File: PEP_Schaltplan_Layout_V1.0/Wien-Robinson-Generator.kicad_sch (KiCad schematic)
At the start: 14 parts, among them Q5 BF256, U13 LT1819

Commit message: Bauoptionen1
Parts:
- removed C24: 100µ, Capacitor_THT:CP_Radial_D13.0mm_P5.00mm, symbol ltspice:cap
- removed Q5: BF256, Package_TO_SOT_THT:TO-92L_Inline, symbol BF256:BF256
- removed R29: 13.75k, Resistor_SMD:R_1206_3216Metric, symbol ltspice:res
- removed R30: 20k, Resistor_SMD:R_1206_3216Metric, symbol ltspice:res
- added C29, C30, C31, C32, C33, C34, C35, C36, C37, C38, C39, C40, C41, C42: 6.8n, Capacitor_SMD:C_1206_3216Metric, symbol ltspice:cap
- added D17: 1N4148, Diode_THT:D_DO-41_SOD81_P10.16mm_Horizontal, symbol ltspice:diode
- added R44: 10k, Resistor_SMD:R_1206_3216Metric, symbol ltspice:res
- added R50, R51, R52, R53, R54: 0, Resistor_SMD:R_1206_3216Metric, symbol ltspice:res
- added RV3: R_Potentiometer_Dual_Separate, Potentiometer_THT:Potentiometer_Piher_T-16H_Double_Horizontal, symbol Device:R_Potentiometer_Dual_Separate
- added SW1, SW2, SW3, SW4, SW5, SW6: SW_DIP_x04, Button_Switch_THT:SW_DIP_SPSTx04_Slide_6.7x11.72mm_W7.62mm_P2.54mm_LowProfile, symbol Switch:SW_DIP_x04
- R27, R31: value 2k2 -> 500
- R28: value 2k -> 10k
- R32: value 20k -> 0
- R33: value 22k -> 24K
- R34: value 16k -> 12k
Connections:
- net 0: now also C29.2, C30.2, C31.2, C32.2, C33.2, C34.2, C35.2, R52.2
- net Sinus: now also D11.2 (-), D17.1 (+), R54.1, SW3.5, SW3.6, SW3.7, SW3.8, SW4.5, SW4.6, SW4.7, SW4.8
- net at R31.2, U13.3 (+): now also RV3.2, SW1.5, SW1.6, SW1.7, SW1.8, SW2.5, SW2.6, SW2.7, SW2.8; no longer C23.1
- net at R34.2: now also R33.2, R44.1
- net at R27.1: now also R50.2
- net at R28.1, U13.2 (-): now also R51.2; no longer R33.2
- net at R28.2: now also R52.1
- net at C25.2: now also SW5.8; no longer R32.1
- net at D11.1 (+): now also D17.2 (-), R53.1; no longer R34.1
- new net: C39.1, SW4.1
- new net: C40.1, SW4.2
- new net: C41.1, SW4.3
- new net: C42.1, SW4.4
- new net: C23.1, SW1.1
- new net: C30.1, SW1.3
- new net: R33.1, R53.2
- new net: C32.1, SW2.1
- new net: C35.1, SW2.4
- new net: C36.1, SW3.2
- new net: C36.2, SW5.7
- new net: C25.1, SW3.1
- new net: R32.1, RV3.4
- new net: RV3.5, SW5.1, SW5.2, SW5.3, SW5.4, SW6.1, SW6.2, SW6.3, SW6.4
- new net: R50.1, RV3.1
- new net: R44.2, R51.1
- new net: C31.1, SW1.4
- new net: C38.2, SW5.5
- new net: C37.2, SW5.6
- new net: C39.2, SW6.8
- new net: C42.2, SW6.5
- new net: C33.1, SW2.2
- new net: C40.2, SW6.7
- new net: C37.1, SW3.3
- new net: C29.1, SW1.2
- new net: R34.1, R54.2
- new net: C38.1, SW3.4
- new net: C34.1, SW2.3
- new net: C41.2, SW6.6
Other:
- moved on the sheet: C23, D11, R27, R28, R31, R33, R34, U13A, U13C

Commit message: Überarbeitung und Bereinigung
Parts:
- renumbered C29 to C10, C30 to C11, C31 to C12, C32 to C13, C33 to C14, C34 to C15, C35 to C16, C25 to C17, C36 to C18, C37 to C19, C38 to C20, C39 to C21, C40 to C22, C41 to C23, C42 to C24, C23 to C9, D11 to D8, D17 to D9, R52 to R10, R28 to R11, R51 to R12, R44 to R13, R31 to R14, R32 to R15, R33 to R16, R34 to R17, R53 to R18, R54 to R19, R27 to R8, R50 to R9, RV3 to RV1, SW5 to SW3, SW6 to SW4, SW3 to SW5, SW4 to SW6, U13 to U4
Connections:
- net Sinus renamed Sinus_Wien
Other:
- note removed: "R2 und R3 sollen als Doppel potenziometer eingestellt werden jedoch noch mit einem festwider stand von 2k2 damit keine 0 Ohm anliegen können"
- moved on the sheet: C10, C11, C12, C13, C14, C15, C16, C17, C18, C19, C20, C21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

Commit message: Pinheads eingefügt, GND überall (hoffentlich angebunden)
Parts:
- added C10, C9: 100n, Capacitor_SMD:C_1206_3216Metric, symbol ltspice:cap
- added J4: Conn_01x01_Pin, Connector_PinSocket_2.54mm:PinSocket_1x01_P2.54mm_Vertical, symbol Connector:Conn_01x01_Pin
- renumbered C9 to C11, C10 to C12, C11 to C13, C12 to C14, C13 to C15, C14 to C16, C15 to C17, C16 to C18, C17 to C19, C18 to C20, C19 to C21, C20 to C22, C21 to C23, C22 to C24, C23 to C25, C24 to C26, D8 to D10, D9 to D11, R9 to R10, R10 to R11, R11 to R12, R12 to R13, R13 to R14, R14 to R15, R15 to R16, R16 to R17, R17 to R18, R18 to R19, R19 to R20, R8 to R9
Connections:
- net +5V: now also C9.1
- net -5V: now also C10.1
- net 0: now also C10.2, C9.2
- net Sinus_Wien: now also J4.1 (Pin_1)

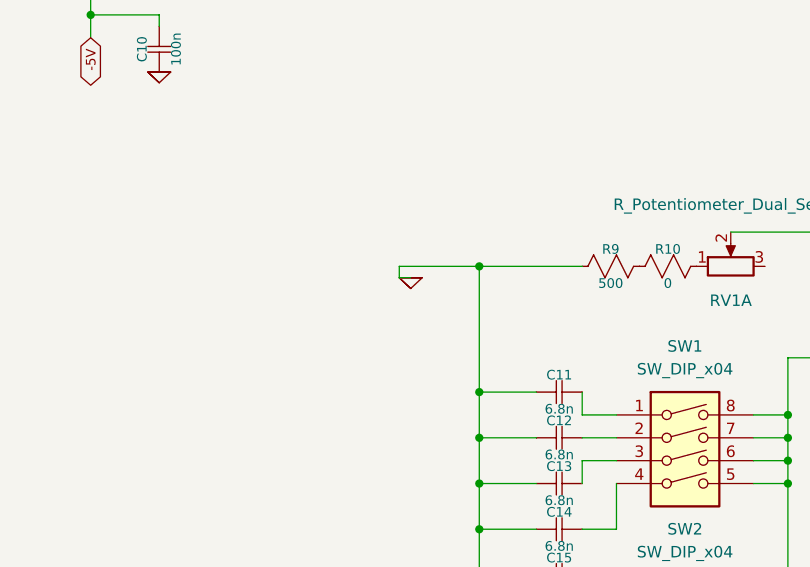
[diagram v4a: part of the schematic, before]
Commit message: Leiterplatten größe definiert und erstes Auto Routing
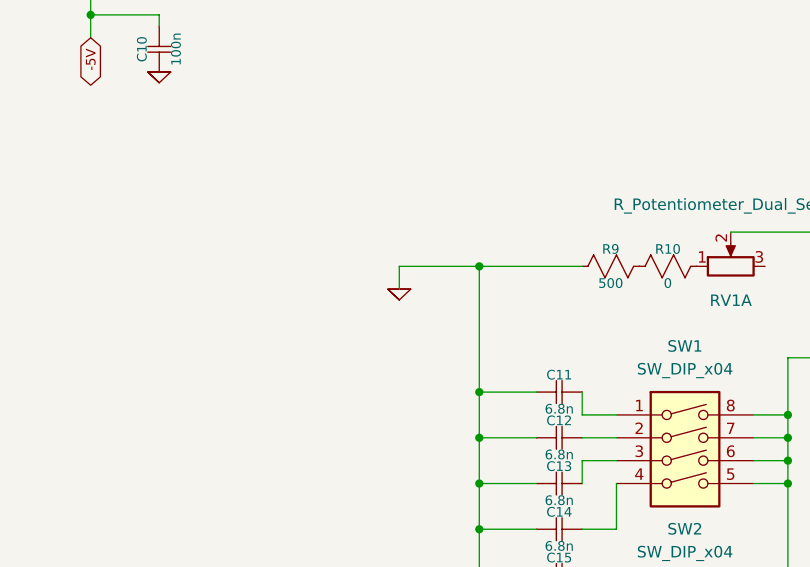
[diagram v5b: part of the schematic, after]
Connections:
- net 0 renamed GND
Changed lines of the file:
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@@
 	(wire
 		(pts
-			(xy 69.85 77.47) (xy 71.12 77.47)
-		)
-		(stroke
-			(width 0.1524)
-			(type solid)
-		)
-	)
-	(wire
-		(pts
 			(xy 229.87 67.31) (xy 229.87 69.85)
 		)
@@
 	(wire
 		(pts
-			(xy 69.85 77.47) (xy 69.85 76.2)
+			(xy 69.85 78.74) (xy 69.85 76.2)
 		)
 		(stroke
@@
 		(at 92.71 135.89 0)
 		(unit 1)
-		(body_style 0)
+		(body_style 1)
 		(exclude_from_sim no)
 		(in_bom yes)
@@
 			)
 		)
-		(property "Value" "0"
+		(property "Value" "GND"
 			(at 92.71 135.89 0)
 			(hide yes)
@@
 	(symbol
 		(lib_id "ltspice:GND")
-		(at 71.12 77.47 0)
+		(at 69.85 78.74 0)
 		(unit 1)
-		(body_style 0)
+		(body_style 1)
 		(exclude_from_sim no)
 		(in_bom yes)
@@
 		(dnp no)
 		(property "Reference" "#GND03"
-			(at 71.12 77.47 0)
+			(at 69.85 78.74 0)
 			(hide yes)
 			(show_name no)
@@
 			)
 		)
-		(property "Value" "0"
-			(at 71.12 77.47 0)
+		(property "Value" "GND"
+			(at 69.85 78.74 0)
 			(hide yes)
 			(show_name no)
@@
 		)
 		(property "Footprint" ""
-			(at 71.12 77.47 0)
+			(at 69.85 78.74 0)
 			(hide yes)
 			(show_name no)
@@
 		)
 		(property "Datasheet" ""
-			(at 71.12 77.47 0)
+			(at 69.85 78.74 0)
 			(hide yes)
 			(show_name no)
@@
 		)
 		(property "Description" ""
-			(at 71.12 77.47 0)
+			(at 69.85 78.74 0)
 			(hide yes)
 			(show_name no)
@@
 		(at 43.18 54.61 0)
 		(unit 1)
-		(body_style 0)
+		(body_style 1)
 		(exclude_from_sim no)
 		(in_bom yes)
@@
 			)
 		)
-		(property "Value" "0"
+		(property "Value" "GND"
 			(at 43.18 54.61 0)
 			(hide yes)
@@
 		(at 43.18 38.1 0)
 		(unit 1)
-		(body_style 0)
+		(body_style 1)
 		(exclude_from_sim no)
 		(in_bom yes)
@@
 			)
 		)
-		(property "Value" "0"
+		(property "Value" "GND"
 			(at 43.18 38.1 0)
 			(hide yes)

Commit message: Anpassung
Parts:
- C11, C19: value 6.8n -> 33p
- C12, C20: value 6.8n -> 68p
- C13, C21: value 6.8n -> 150p
- C14, C22: value 6.8n -> 330p
- C15: value 6.8n -> 680n
- C17, C24: value 6.8n -> 1n
- C18, C26: value 6.8n -> 4.7n
- C23: value 6.8n -> 680p
- C25: value 6.8n -> 2.2n
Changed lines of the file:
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@@
 			)
 		)
-		(property "Value" "6.8n"
+		(property "Value" "33p"
 			(at 87.63 91.44 90)
 			(show_name no)
@@
 			)
 		)
-		(property "Value" "6.8n"
+		(property "Value" "150p"
 			(at 87.63 101.6 90)
 			(show_name no)
@@
 			)
 		)
-		(property "Value" "6.8n"
+		(property "Value" "680n"
 			(at 87.63 111.76 90)
 			(show_name no)
@@
 			)
 		)
-		(property "Value" "6.8n"
+		(property "Value" "4.7n"
 			(at 87.63 127 90)
 			(show_name no)
@@
 			)
 		)
-		(property "Value" "6.8n"
+		(property "Value" "68p"
 			(at 201.93 48.26 90)
 			(show_name no)
@@
 			)
 		)
-		(property "Value" "6.8n"
+		(property "Value" "33p"
 			(at 201.93 43.18 90)
 			(show_name no)
@@
 			)
 		)
-		(property "Value" "6.8n"
+		(property "Value" "330p"
 			(at 87.63 106.68 90)
 			(show_name no)
@@
 			)
 		)
-		(property "Value" "6.8n"
+		(property "Value" "680p"
 			(at 201.93 63.5 90)
 			(show_name no)
@@
 			)
 		)
-		(property "Value" "6.8n"
+		(property "Value" "4.7n"
 			(at 201.93 78.74 90)
 			(show_name no)
@@
 			)
 		)
-		(property "Value" "6.8n"
+		(property "Value" "1n"
 			(at 201.93 68.58 90)
 			(show_name no)
@@
 			)
 		)
-		(property "Value" "6.8n"
+		(property "Value" "150p"
 			(at 201.93 53.34 90)
 			(show_name no)
@@
 			)
 		)
-		(property "Value" "6.8n"
+		(property "Value" "68p"
 			(at 87.63 96.52 90)
 			(show_name no)
@@
 			)
 		)
-		(property "Value" "6.8n"
+		(property "Value" "330p"
 			(at 201.93 58.42 90)
 			(show_name no)
@@
 			)
 		)
-		(property "Value" "6.8n"
+		(property "Value" "1n"
 			(at 87.63 121.92 90)
 			(show_name no)
@@
 			)
 		)
-		(property "Value" "6.8n"
+		(property "Value" "2.2n"
 			(at 201.93 73.66 90)
 			(show_name no)

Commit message: Upps vergessen
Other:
- note added: "Ein 100K Ohm Widerstand vor R12 gegen masse"
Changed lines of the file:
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@@
 		(company "TH Mannheim")
 	)
+	(text "Ein 100K Ohm Widerstand vor R12 gegen masse\n"
+		(exclude_from_sim no)
+		(at 118.618 137.922 0)
+		(effects
+			(font
+				(size 1.27 1.27)
+			)
+		)
+	)
 	(junction
 		(at 229.87 52.07)
@@
 	)
 	(junction
+		(at 123.19 132.08)
+		(diameter 0)
+		(color 0 0 0 0)
+	)
+	(junction
 		(at 229.87 64.77)
 		(diameter 0)
@@
 		(diameter 0)
 		(color 0 0 0 0)
-	)
-	(junction
-		(at 123.19 132.08)
-		(diameter 0)
-		(color 0 0 0 0)
